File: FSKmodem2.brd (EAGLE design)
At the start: 32.1 x 16.5 mm, 9 parts, among them IC1 TCM3105

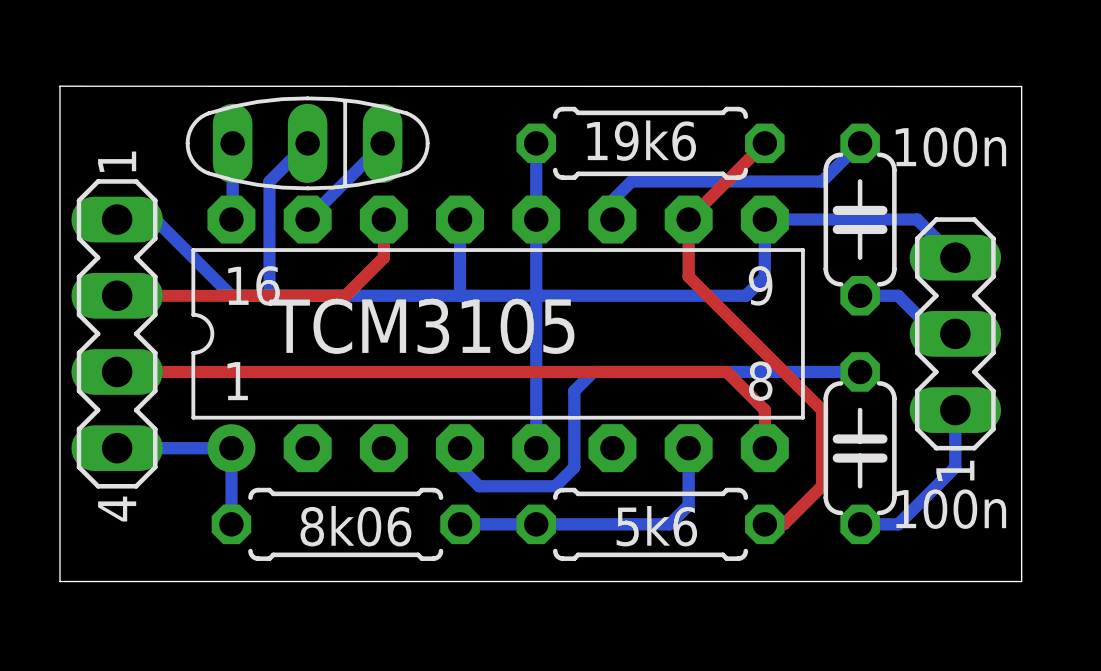
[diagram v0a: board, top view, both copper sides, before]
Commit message: Fixing the resistors, they were so wrong
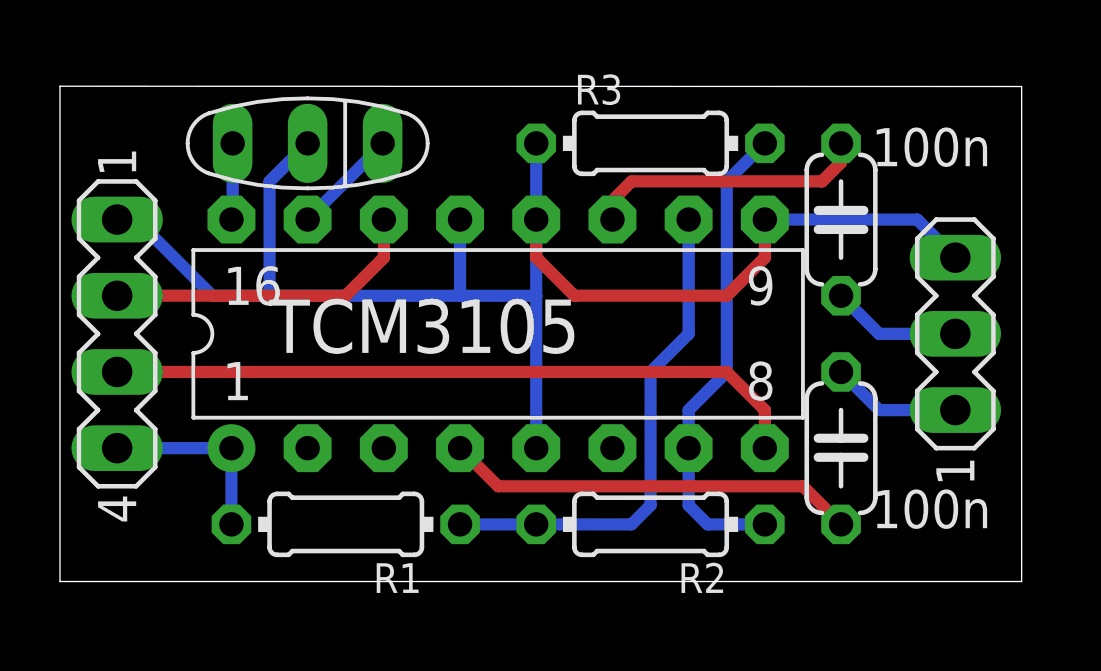
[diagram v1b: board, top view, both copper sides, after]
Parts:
- R1: value 8k06 -> 18k; device rcl:0207/7 -> rcl:0204/7
- R2: device rcl:0207/7 -> rcl:0204/7
- R3: value 19k6 -> 33k; device rcl:0207/7 -> rcl:0204/7
- moved C1 0.64 mm to (26.0, 4.45), turned to 90 degrees
- moved C2 0.64 mm to (26.0, 12.1)
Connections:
- removed net N$10: IC1.7, R1.1, R2.2
- removed net N$11: IC1.10, R2.1, R3.2
- new net N$1: IC1.10, R1.1, R2.2
- new net N$7: IC1.7, R2.1, R3.2
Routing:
- net N$11: track 16.8 -> 0.00 mm
- net N$1: track 0.00 -> 16.7 mm
- net N$7: track 0.00 -> 15.9 mm
- net N$10: track 9.79 -> 0.00 mm
- net N$4: track 17.3 -> 13.8 mm
- net N$6: track 5.87 -> 4.34 mm
- net GND: track 50.0 -> 51.4 mm
- net N$3: track 3.70 -> 4.34 mm
